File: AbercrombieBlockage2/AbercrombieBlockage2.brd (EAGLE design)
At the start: 38 x 30 mm, 35 parts, among them U1 DMN3135LVT, U2 ICS-43434, U3 CYBLE-022001-00, U4 LIS3DH, U5 VL53L0X, U6 VL53L0X, U7 VL53L0X, U8 M24

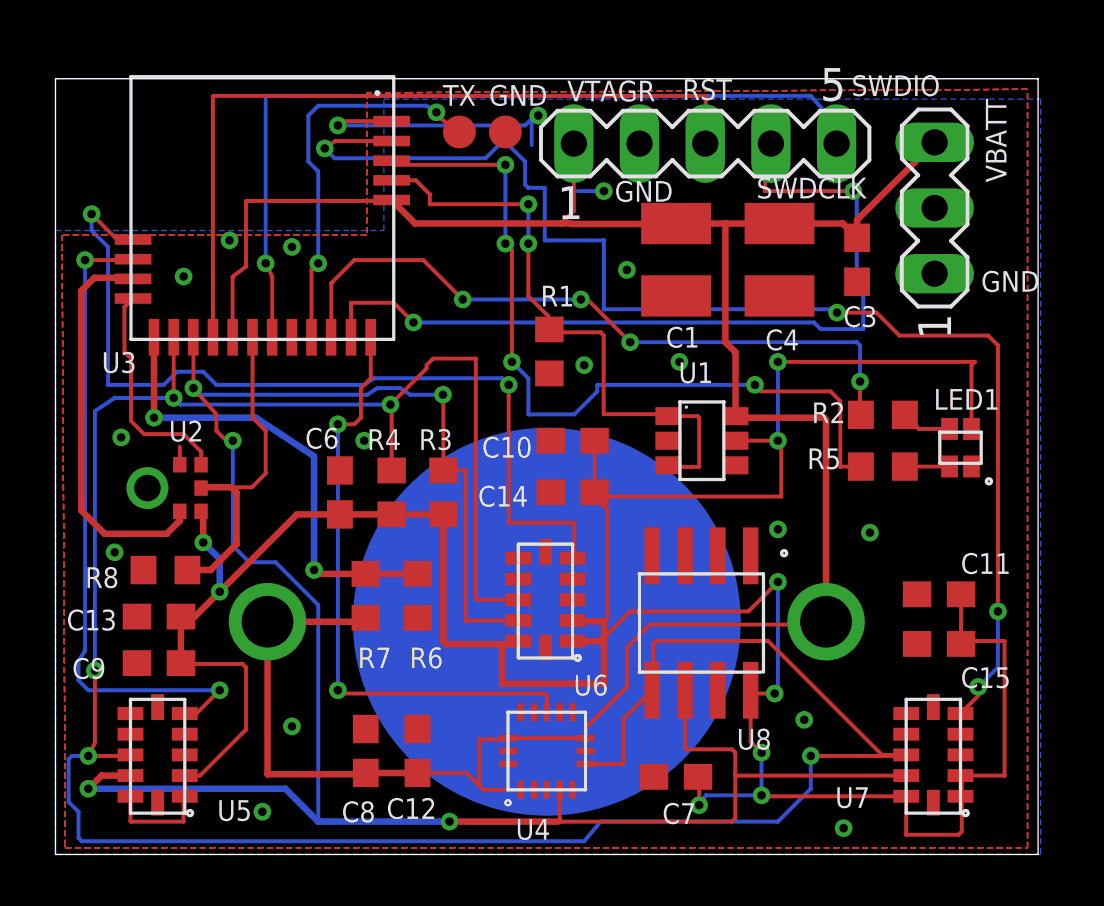
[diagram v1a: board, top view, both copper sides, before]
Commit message: Updated some issues with the Abercrombie Gen4 spray system. Completely re-routed the design.
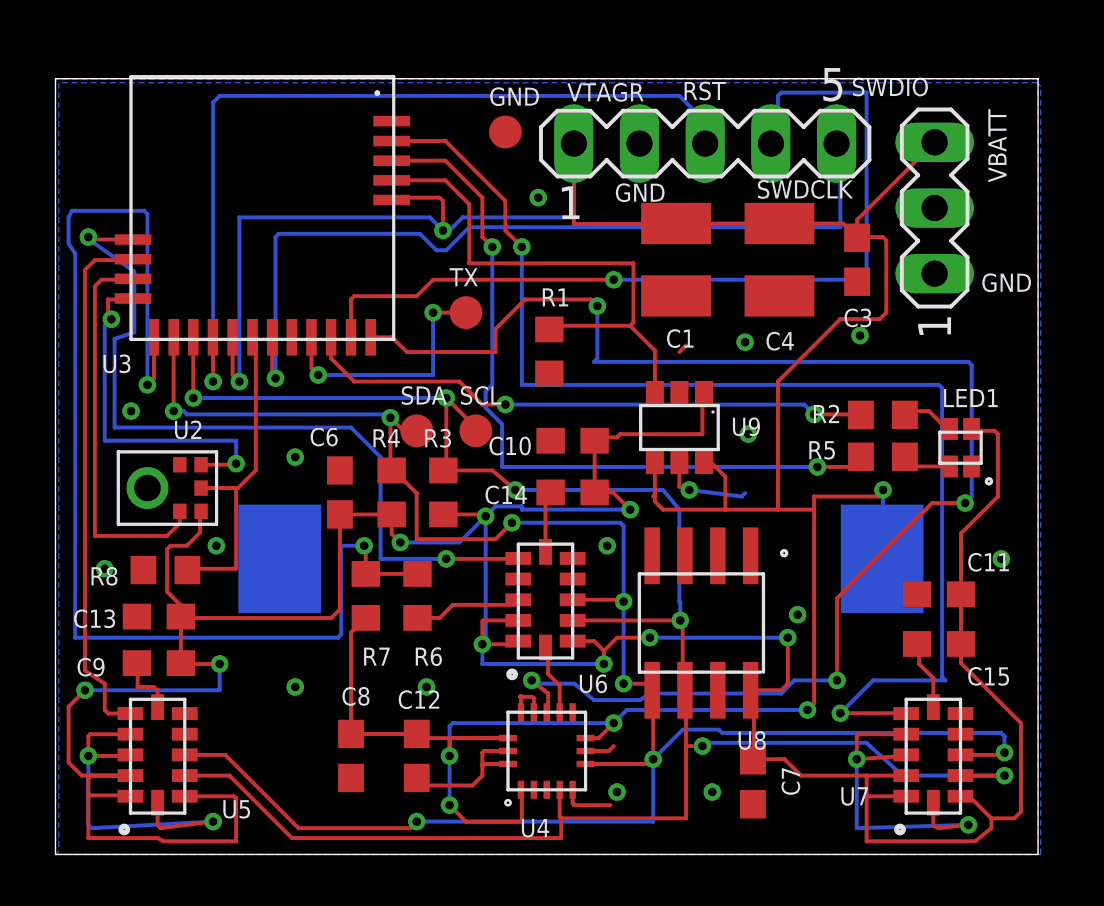
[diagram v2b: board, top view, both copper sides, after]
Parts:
- removed BAT1: (no value), NicksParts:COIN_CELL
- removed U1: DMN3135LVT, NicksParts:SOT-23-6
- added B1: (no value), NicksParts:BU2032
- added SCL, SDA: TPB1,27, testpad:B1,27
- added U9: (no value), NicksParts:SOT-23-6
- moved TX 6.99 mm to (15.9, 21.0)
- moved C7 2.98 mm to (27.0, 2.79), turned to 270 degrees
- moved C8 0.60 mm to (11.4, 3.81), turned to 270 degrees
- moved R5 0.38 mm to (32.0, 15.4)
- moved C12 0.19 mm to (14.0, 3.81), turned to 270 degrees
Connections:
- net GND: now also B1.NEG, U9.2, U9.5; no longer BAT1.GND1
- net PWR_EN: now also U9.3; no longer U1.1, U1.3
- net SCL: now also SCL.TP
- net SDA: now also SDA.TP
- net V+: now also U9.1; no longer U1.5
- net VDD: now also B1.PLUS, U9.4, U9.6; no longer BAT1.VPLUS1, BAT1.VPLUS2, U1.6
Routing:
- net GND: track 13.1 -> 58.0 mm, vias 18 -> 20
- net WAKEUP: track 23.4 -> 57.2 mm, vias 2 -> 4
- net VBATT: track 18.2 -> 45.9 mm
- net VDD: track 95.1 -> 122.0 mm, vias 0 -> 7
- net SDA: track 103.4 -> 79.7 mm, vias 5 -> 8
- net V+: track 122.8 -> 134.5 mm
- net UART_TX: track 15.2 -> 9.69 mm
- net SCL: track 85.2 -> 79.8 mm, vias 5 -> 6
- net WS: track 8.69 -> 13.9 mm, vias 0 -> 2
- net XSHUT_1: track 25.5 -> 20.5 mm, vias 2 -> 0
- net BLUE_LED: track 27.0 -> 22.2 mm, vias 4 -> 2
- net XSHUT_2: track 34.3 -> 30.6 mm
- net PWR_EN: track 23.8 -> 20.7 mm, vias 2 -> 0
- net XSHUT_3: track 50.5 -> 47.5 mm, vias 4 -> 2
- net XRES: track 30.2 -> 32.9 mm, vias 0 -> 1
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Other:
- board text added: "Abercrombie BLE LaserSpray V2 Appareo Systems 2016"
- board text removed: "Abercrombie BLE LaserSpray V1.0 Appareo Systems 2016"

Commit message: Minor updates to the layout.
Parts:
- C4: value 10u -> 220u
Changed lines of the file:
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@@
 <layer number="37" name="tTest" color="7" fill="1" visible="no" active="yes"/>
 <layer number="38" name="bTest" color="7" fill="1" visible="no" active="yes"/>
-<layer number="39" name="tKeepout" color="4" fill="11" visible="no" active="yes"/>
+<layer number="39" name="tKeepout" color="4" fill="11" visible="yes" active="yes"/>
 <layer number="40" name="bKeepout" color="1" fill="11" visible="no" active="yes"/>
-<layer number="41" name="tRestrict" color="4" fill="10" visible="no" active="yes"/>
+<layer number="41" name="tRestrict" color="4" fill="10" visible="yes" active="yes"/>
 <layer number="42" name="bRestrict" color="1" fill="10" visible="no" active="yes"/>
 <layer number="43" name="vRestrict" color="2" fill="10" visible="no" active="yes"/>
@@
 <rectangle x1="17.9" y1="7.6" x2="20" y2="12" layer="41"/>
 <rectangle x1="33" y1="1.6" x2="35" y2="6" layer="41"/>
+<rectangle x1="17.526" y1="2.413" x2="20.447" y2="5.461" layer="41"/>
 </plain>
 <attributes>
@@
 <attribute name="DIGIKEYY" value="490-13250-1-ND" x="24" y="23" size="1.778" layer="27" rot="R270" display="off"/>
 </element>
-<element name="C4" library="resistor" package="C1210" value="10u" x="28" y="23" smashed="yes" rot="R270">
+<element name="C4" library="resistor" package="C1210" value="220u" x="28" y="23" smashed="yes" rot="R270">
 <attribute name="NAME" x="27.448" y="19.5" size="0.7" layer="25"/>
 <attribute name="VALUE" x="26.857" y="27.826" size="0.7" layer="27" rot="R270"/>
@@
 <wire x1="26.543" y1="13.843" x2="26.67" y2="13.97" width="0.1524" layer="16"/>
 <via x="1.905" y="11.049" extent="1-16" drill="0.3302"/>
+<wire x1="19.5" y1="5.5" x2="18.5" y2="5.5" width="0" layer="19" extent="1-1"/>
 </signal>
 <signal name="XRES">

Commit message: Order V2 of the Gen4 spray pattern monitor.
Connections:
- net GND: no longer U8.1
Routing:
- net GND: track 58.0 -> 56.1 mm, vias 20 -> 21
- net WAKEUP: track 57.2 -> 55.7 mm
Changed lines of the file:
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@@
 <layer number="37" name="tTest" color="7" fill="1" visible="no" active="yes"/>
 <layer number="38" name="bTest" color="7" fill="1" visible="no" active="yes"/>
-<layer number="39" name="tKeepout" color="4" fill="11" visible="yes" active="yes"/>
+<layer number="39" name="tKeepout" color="4" fill="11" visible="no" active="yes"/>
 <layer number="40" name="bKeepout" color="1" fill="11" visible="no" active="yes"/>
-<layer number="41" name="tRestrict" color="4" fill="10" visible="yes" active="yes"/>
+<layer number="41" name="tRestrict" color="4" fill="10" visible="no" active="yes"/>
 <layer number="42" name="bRestrict" color="1" fill="10" visible="no" active="yes"/>
 <layer number="43" name="vRestrict" color="2" fill="10" visible="no" active="yes"/>
@@
 <contactref element="C11" pad="2"/>
 <contactref element="C15" pad="2"/>
-<contactref element="U8" pad="1"/>
 <contactref element="U8" pad="2"/>
 <contactref element="U8" pad="3"/>
@@
 <wire x1="20.5" y1="4" x2="21.399" y2="4" width="0.1524" layer="1"/>
 <wire x1="21.399" y1="4" x2="21.59" y2="4.191" width="0.1524" layer="1"/>
-<wire x1="19.5" y1="5.5" x2="19.5" y2="6.535" width="0.1524" layer="1"/>
-<wire x1="19.5" y1="6.535" x2="19.05" y2="6.985" width="0.1524" layer="1"/>
-<wire x1="19.05" y1="6.985" x2="19.05" y2="7.9" width="0.1524" layer="1"/>
-<wire x1="19.05" y1="7.9" x2="18.95" y2="8" width="0.1524" layer="1"/>
 <wire x1="14" y1="9.15" x2="14.865" y2="9.15" width="0.1524" layer="1"/>
 <wire x1="14.865" y1="9.15" x2="15.367" y2="9.652" width="0.1524" layer="1"/>
@@
 <wire x1="26.543" y1="13.843" x2="26.67" y2="13.97" width="0.1524" layer="16"/>
 <via x="1.905" y="11.049" extent="1-16" drill="0.3302"/>
-<wire x1="19.5" y1="5.5" x2="18.5" y2="5.5" width="0" layer="19" extent="1-1"/>
+<wire x1="19.5" y1="5.5" x2="19.5" y2="6.292" width="0.1524" layer="1"/>
+<wire x1="19.5" y1="6.292" x2="19.558" y2="6.35" width="0.1524" layer="1"/>
+<via x="20.828" y="5.842" extent="1-16" drill="0.3302"/>
 </signal>
 <signal name="XRES">
@@
 <wire x1="30.226" y1="6.731" x2="28.575" y2="6.731" width="0.1524" layer="16"/>
 <wire x1="28.575" y1="6.731" x2="28.067" y2="6.223" width="0.1524" layer="16"/>
-<wire x1="19.05" y1="6.223" x2="18.415" y2="6.731" width="0.1524" layer="16"/>
-<via x="18.415" y="6.731" extent="1-16" drill="0.3302"/>
-<wire x1="18.415" y1="6.731" x2="19.05" y2="6.223" width="0.1524" layer="1"/>
-<wire x1="19.05" y1="6.223" x2="19.05" y2="5.55" width="0.1524" layer="1"/>
-<wire x1="19.05" y1="5.55" x2="19" y2="5.5" width="0.1524" layer="1"/>
+<via x="21.209" y="6.604" extent="1-16" drill="0.3302"/>
 <wire x1="28.067" y1="6.223" x2="22.987" y2="6.223" width="0.1524" layer="16"/>
 <wire x1="22.987" y1="6.223" x2="22.606" y2="5.969" width="0.1524" layer="16"/>
-<wire x1="22.606" y1="5.969" x2="20.828" y2="5.969" width="0.1524" layer="16"/>
-<wire x1="20.828" y1="5.969" x2="20.066" y2="6.604" width="0.1524" layer="16"/>
-<wire x1="20.066" y1="6.604" x2="18.542" y2="6.604" width="0.1524" layer="16"/>
-<wire x1="18.542" y1="6.604" x2="18.415" y2="6.731" width="0.1524" layer="16"/>
+<wire x1="22.606" y1="5.969" x2="21.844" y2="5.969" width="0.1524" layer="16"/>
+<wire x1="21.209" y1="6.604" x2="21.209" y2="6.35" width="0.1524" layer="16"/>
+<wire x1="21.209" y1="6.35" x2="21.844" y2="5.969" width="0.1524" layer="16"/>
+<wire x1="19.05" y1="5.55" x2="19" y2="5.5" width="0.1524" layer="1"/>
+<wire x1="19.05" y1="5.55" x2="19.05" y2="6.858" width="0.1524" layer="1"/>
+<wire x1="19.05" y1="6.858" x2="20.955" y2="6.858" width="0.1524" layer="1"/>
+<wire x1="20.955" y1="6.858" x2="21.209" y2="6.604" width="0.1524" layer="1"/>
 </signal>
 <signal name="XSHUT_3">
@@
 <wire x1="23.114" y1="6.311" x2="23.075" y2="6.35" width="0.1524" layer="1"/>
 <wire x1="20" y1="9.85" x2="21.9" y2="9.85" width="0.1524" layer="1"/>
-<wire x1="21.9" y1="9.85" x2="21.971" y2="9.779" width="0.1524" layer="1"/>
-<via x="21.971" y="9.779" extent="1-16" drill="0.3302"/>
-<wire x1="21.971" y1="9.779" x2="21.971" y2="6.604" width="0.1524" layer="16"/>
-<via x="21.971" y="6.604" extent="1-16" drill="0.3302"/>
+<wire x1="21.9" y1="9.85" x2="22.098" y2="9.779" width="0.1524" layer="1"/>
+<via x="22.098" y="9.779" extent="1-16" drill="0.3302"/>
+<wire x1="22.098" y1="9.779" x2="22.098" y2="6.604" width="0.1524" layer="16"/>
+<via x="22.098" y="6.604" extent="1-16" drill="0.3302"/>
 <wire x1="5" y1="3.85" x2="6.564" y2="3.85" width="0.1524" layer="1"/>
 <wire x1="6.564" y1="3.85" x2="9.398" y2="1.016" width="0.1524" layer="1"/>
@@
 <wire x1="17.018" y1="12.192" x2="17.653" y2="12.827" width="0.1524" layer="1"/>
 <via x="17.653" y="12.827" extent="1-16" drill="0.3302"/>
-<wire x1="17.653" y1="12.827" x2="21.844" y2="12.827" width="0.1524" layer="16"/>
-<wire x1="21.844" y1="12.827" x2="21.971" y2="12.7" width="0.1524" layer="16"/>
-<wire x1="21.971" y1="12.7" x2="21.971" y2="9.779" width="0.1524" layer="16"/>
 <wire x1="35" y1="3.85" x2="36.616" y2="3.85" width="0.1524" layer="1"/>
 <wire x1="36.616" y1="3.85" x2="36.703" y2="3.937" width="0.1524" layer="1"/>
@@
 <wire x1="5.08" y1="17.018" x2="12.827" y2="17.018" width="0.1524" layer="16"/>
 <wire x1="12.827" y1="17.018" x2="12.954" y2="16.891" width="0.1524" layer="16"/>
-<wire x1="21.971" y1="6.604" x2="22.821" y2="6.604" width="0.1524" layer="1"/>
+<wire x1="22.098" y1="6.604" x2="22.821" y2="6.604" width="0.1524" layer="1"/>
 <wire x1="22.821" y1="6.604" x2="23.075" y2="6.35" width="0.1524" layer="1"/>
+<wire x1="22.098" y1="9.779" x2="22.098" y2="12.192" width="0.1524" layer="16"/>
+<wire x1="22.098" y1="12.192" x2="21.717" y2="12.573" width="0.1524" layer="16"/>
+<wire x1="21.717" y1="12.573" x2="21.463" y2="12.573" width="0.1524" layer="16"/>
+<wire x1="21.463" y1="12.573" x2="21.209" y2="12.827" width="0.1524" layer="16"/>
+<wire x1="21.209" y1="12.827" x2="17.653" y2="12.827" width="0.1524" layer="16"/>
 </signal>
 <signal name="VBATT">
@@
 <wire x1="20" y1="8.25" x2="20.833" y2="8.25" width="0.1524" layer="1"/>
 <wire x1="20.833" y1="8.25" x2="21.209" y2="7.874" width="0.1524" layer="1"/>
-<via x="21.209" y="7.366" extent="1-16" drill="0.3302"/>
-<wire x1="21.209" y1="7.366" x2="16.51" y2="7.366" width="0.1524" layer="16"/>
-<wire x1="16.51" y1="7.366" x2="16.51" y2="8.128" width="0.1524" layer="16"/>
+<via x="21.209" y="7.493" extent="1-16" drill="0.3302"/>
+<wire x1="21.209" y1="7.493" x2="16.51" y2="7.493" width="0.1524" layer="16"/>
+<wire x1="16.51" y1="7.493" x2="16.51" y2="8.128" width="0.1524" layer="16"/>
 <via x="16.51" y="8.128" extent="1-16" drill="0.3302"/>
 <wire x1="16.51" y1="8.128" x2="17.778" y2="8.128" width="0.1524" layer="1"/>
@@
 <wire x1="36.322" y1="16.383" x2="35.497" y2="16.383" width="0.1524" layer="1"/>
 <wire x1="35.497" y1="16.383" x2="35.425" y2="16.455" width="0.1524" layer="1"/>
-<wire x1="21.209" y1="7.366" x2="21.209" y2="7.874" width="0.1524" layer="1"/>
+<wire x1="21.209" y1="7.493" x2="21.209" y2="7.874" width="0.1524" layer="1"/>
 <wire x1="21.209" y1="7.874" x2="21.717" y2="8.382" width="0.1524" layer="1"/>
 <wire x1="21.717" y1="8.382" x2="22.987" y2="8.382" width="0.1524" layer="1"/>

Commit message: Added a readme indicated the Abercrombie projects have been moved.
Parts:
- R6: value 2M -> 301K
- R7: value 6.6M -> 1M
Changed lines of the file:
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@@
 <attribute name="VALUE" x="16.764" y="27.178" size="0.7" layer="27"/>
 </element>
-<element name="R6" library="resistor" package="R0603" value="2M" x="14" y="10" smashed="yes" rot="R270">
+<element name="R6" library="resistor" package="R0603" value="301K" x="14" y="10" smashed="yes" rot="R270">
 <attribute name="NAME" x="15" y="8" size="0.7" layer="25" rot="R180"/>
 <attribute name="VALUE" x="12.095" y="10.635" size="0.7" layer="27" rot="R270"/>
 </element>
-<element name="R7" library="resistor" package="R0603" value="6.6M" x="12" y="10" smashed="yes" rot="R90">
+<element name="R7" library="resistor" package="R0603" value="1M" x="12" y="10" smashed="yes" rot="R90">
 <attribute name="NAME" x="13" y="8" size="0.7" layer="25" rot="R180"/>
 <attribute name="VALUE" x="13.905" y="9.365" size="0.7" layer="27" rot="R90"/>
